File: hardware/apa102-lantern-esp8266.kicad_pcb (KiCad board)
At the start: 2 copper layers, 63.5 x 63.5 mm, 26 parts, among them P1 CONN_01X02, P10 CONN_01X06, P2 CONN_01X06, P3 CONN_01X06, P4 CONN_01X06, P5 CONN_01X06, P6 CONN_01X06, P7 CONN_01X06, P8 CONN_01X06, P9 CONN_01X06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

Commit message: Adds github url to pcbs
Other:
- board text added: "github.com/ Nervengift/ apa102lantern"
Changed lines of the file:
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@@
 (kicad_pcb (version 4) (host pcbnew "(2015-09-28 BZR 6225)-product")
   (general
-    (links 0)
-    (no_connects 0)
+    (links 55)
+    (no_connects 1)
     (area 133.299999 63.449999 196.900001 127.050001)
     (thickness 1.6)
-    (drawings 16)
+    (drawings 17)
     (tracks 141)
     (zones 0)
@@
       (net 2 GND))
   )
+  (gr_text "github.com/\nNervengift/\napa102lantern" (at 165.1 123.19) (layer B.SilkS)
+    (effects (font (size 1 1) (thickness 0.1)) (justify mirror))
+  )
   (gr_text 5V (at 180.721 91.44) (layer B.SilkS)

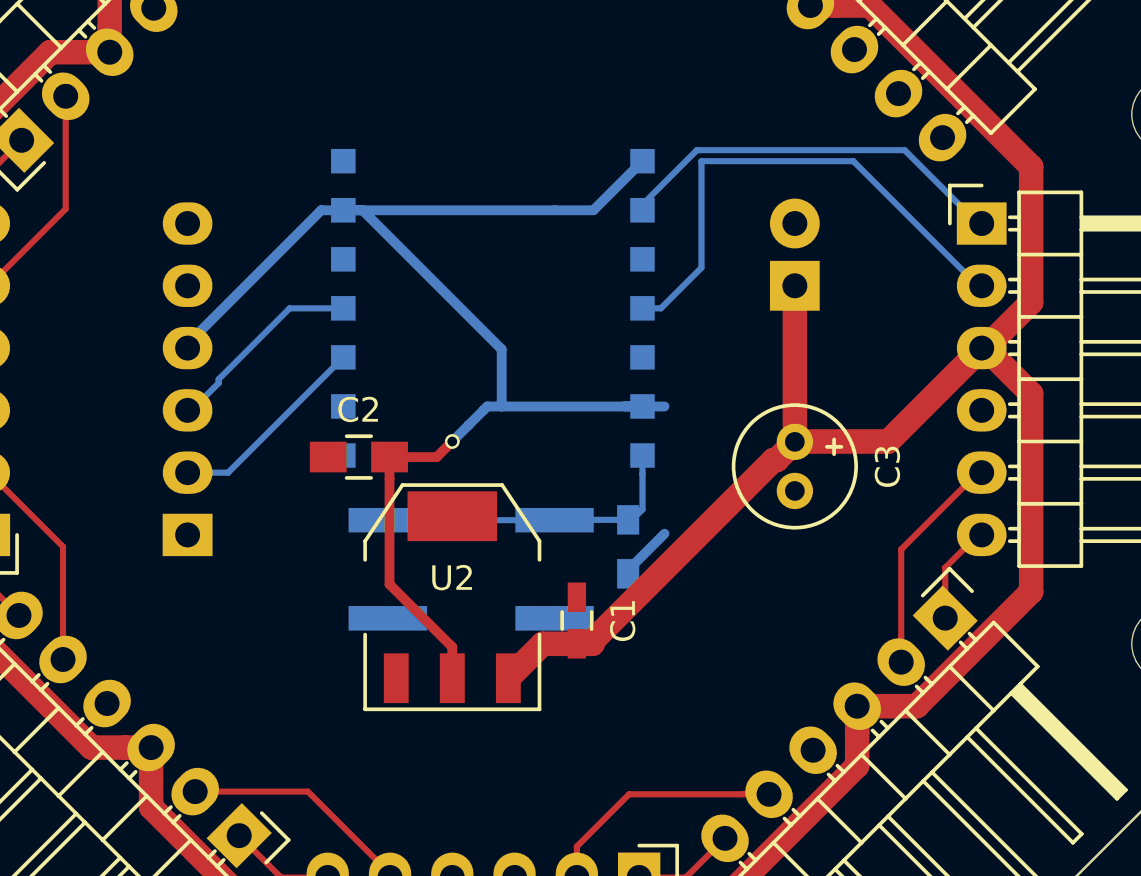
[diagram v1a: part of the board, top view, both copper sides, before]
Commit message: Adds pins to access the leds directly via SPI
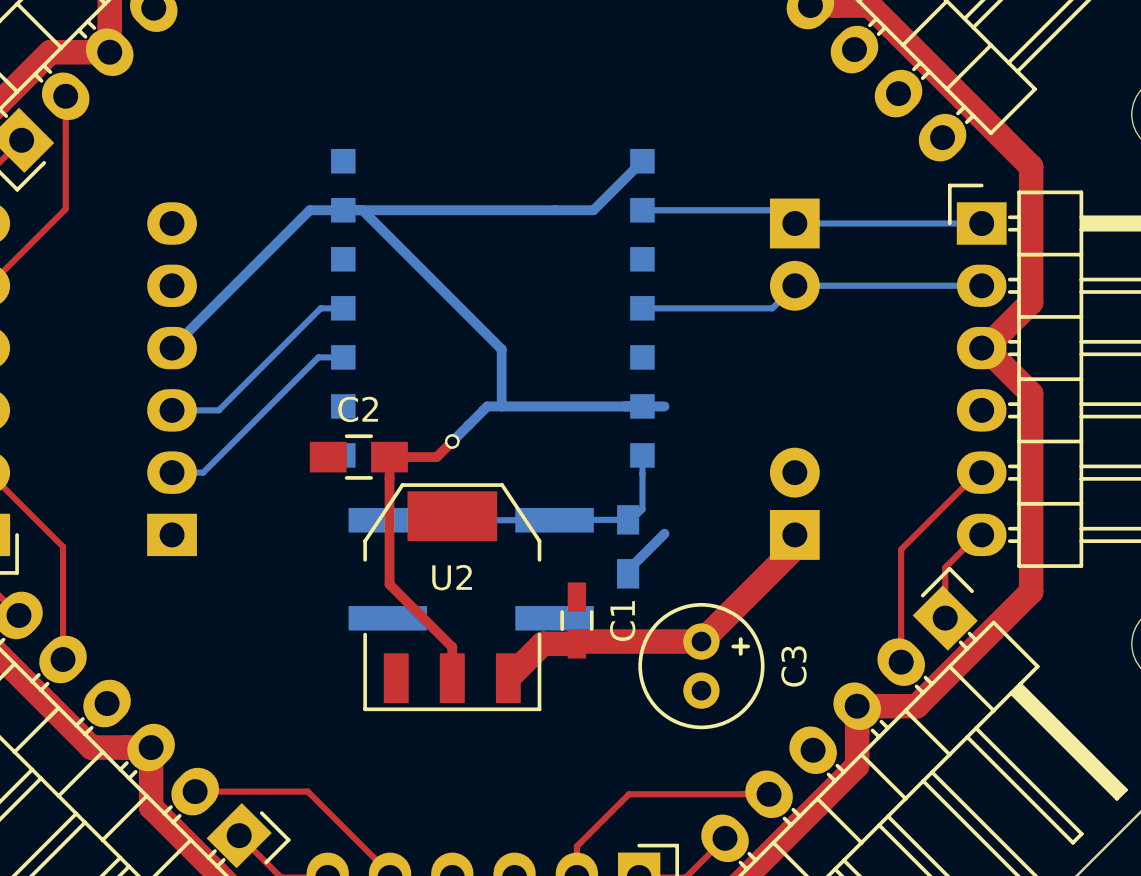
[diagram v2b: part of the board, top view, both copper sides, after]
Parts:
- added P11: CONN_01X02, Pin_Headers:Pin_Header_Straight_1x02, B.Cu at (177.8, 88.9)
- moved P1 10.2 mm to (177.8, 101.6)
- moved C3 8.99 mm to (174.0, 105.9)
- moved P2 0.63 mm to (152.4, 101.6)
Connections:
- net Net-(P3-Pad1) renamed /CLK
- net Net-(P3-Pad2) renamed /MOSI
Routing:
- net VCC: track 189.9 -> 173.1 mm
- net /MOSI: track 21.0 -> 14.4 mm
- net /CLK: track 16.2 -> 14.2 mm
- net /TX: track 8.30 -> 8.93 mm
- net /RX: track 8.16 -> 8.71 mm
- net +3V3: track 58.1 -> 58.6 mm
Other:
- net class 3v3 added: clearance 0.2, trace_width 0.4, via_dia 0.6, via_drill 0.4
- net class Default: trace_width 0.4 -> 0.25
- board text added: "CLK"
- board text added: "DATA"

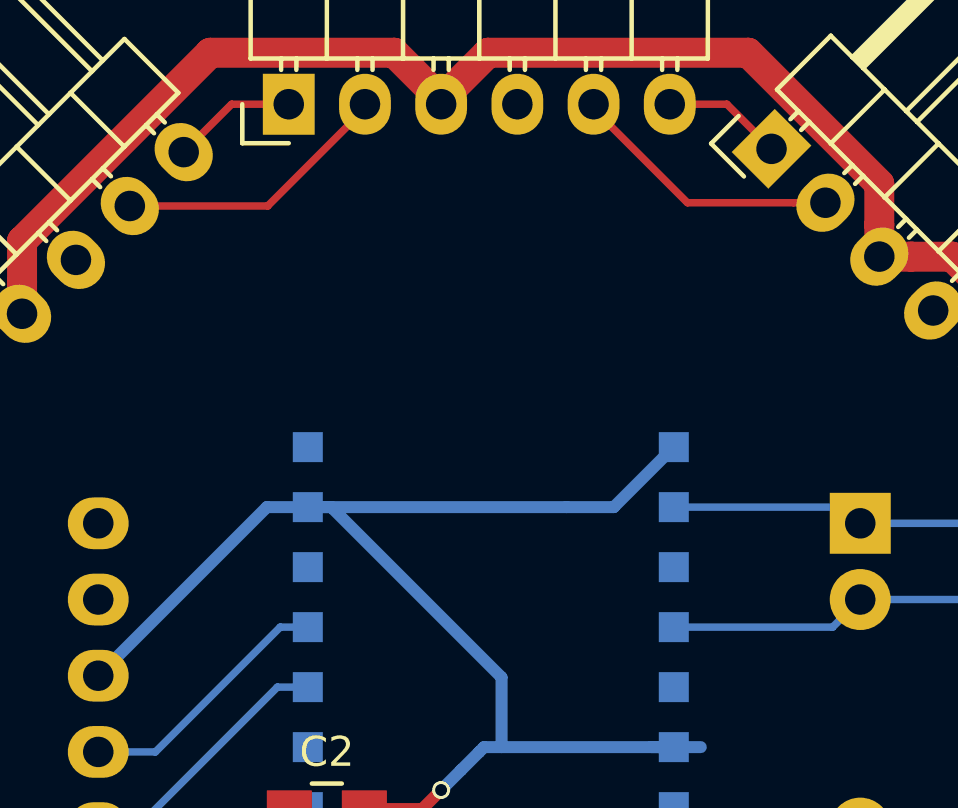
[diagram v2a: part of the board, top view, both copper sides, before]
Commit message: Adds license to esp board silkscreen
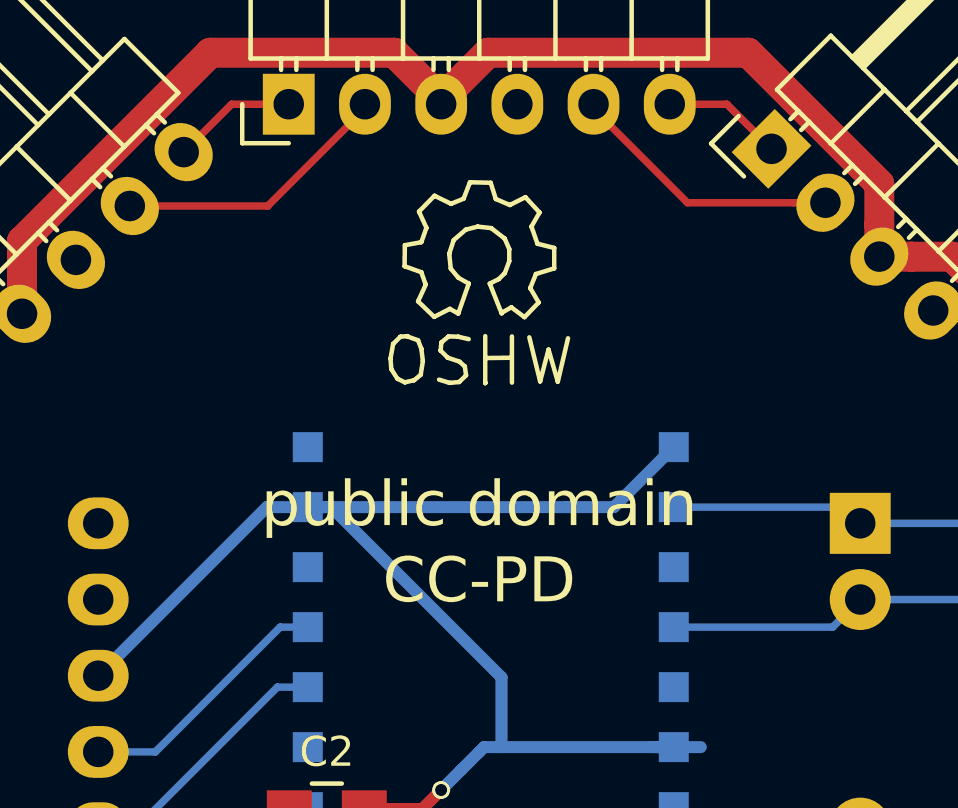
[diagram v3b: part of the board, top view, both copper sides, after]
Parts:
- REF**: moved to F.Cu
- moved REF** 29.2 mm to (165.1, 80.0), turned to 0 degrees
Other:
- board text added: "CC-PD"
- board text added: "public domain"

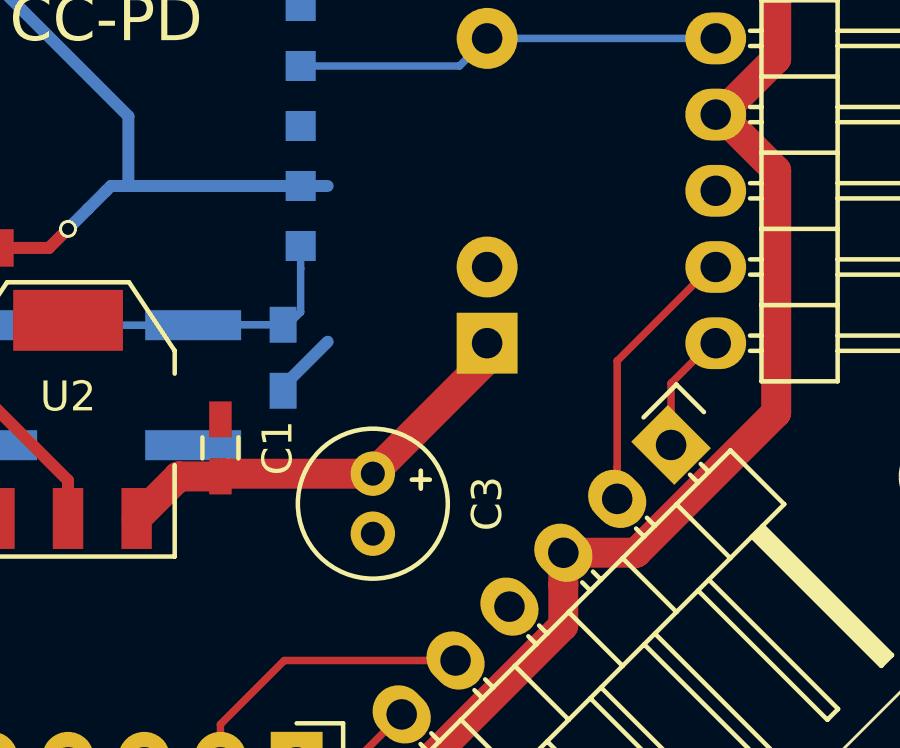
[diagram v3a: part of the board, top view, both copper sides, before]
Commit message: Fixes traces that where lost somehow
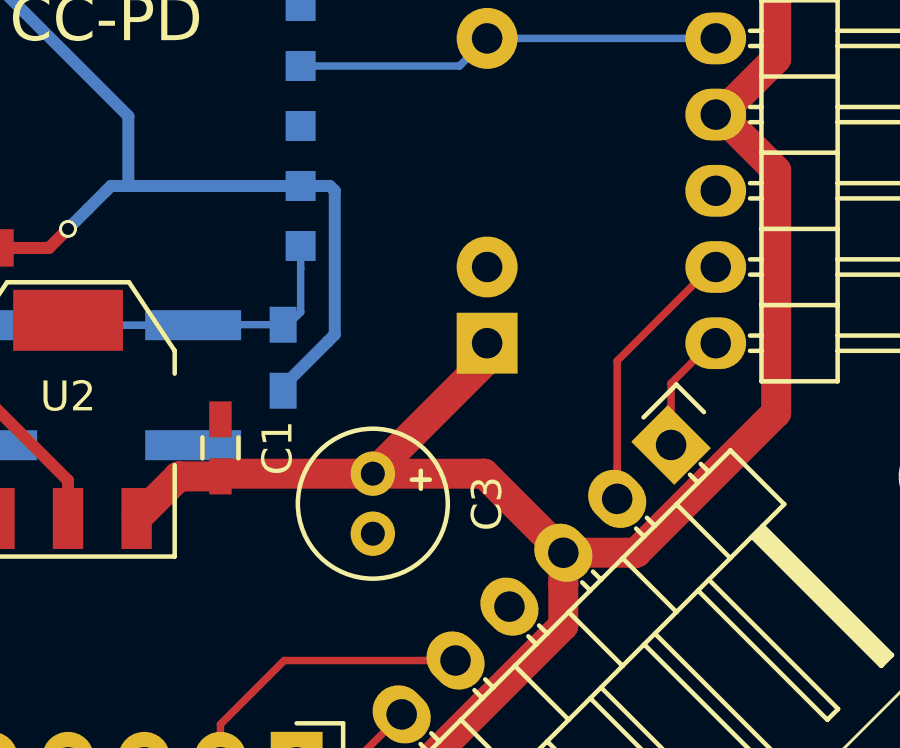
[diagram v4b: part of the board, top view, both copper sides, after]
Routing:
- net VCC: track 173.1 -> 180.5 mm
- net +3V3: track 58.6 -> 64.0 mm
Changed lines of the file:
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@@
 (kicad_pcb (version 4) (host pcbnew "(2015-09-28 BZR 6225)-product")
   (general
-    (links 0)
-    (no_connects 2)
+    (links 57)
+    (no_connects 0)
     (area 133.299999 63.449999 196.900001 127.050001)
     (thickness 1.6)
     (drawings 21)
-    (tracks 132)
+    (tracks 138)
     (zones 0)
     (modules 27)
@@
   (gr_line (start 177.8 127) (end 196.85 107.95) (layer Edge.Cuts) (width 0.1))
   (gr_line (start 152.4 127) (end 177.8 127) (layer Edge.Cuts) (width 0.1))
+  (segment (start 173.99 105.94848) (end 177.70348 105.94848) (width 1) (layer F.Cu) (net 1))
+  (segment (start 177.70348 105.94848) (end 180.34 108.585) (width 1) (layer F.Cu) (net 1))
   (segment (start 173.99 105.94848) (end 169.00152 105.94848) (width 1) (layer F.Cu) (net 1))
   (segment (start 169.00152 105.94848) (end 168.91 106.04) (width 1) (layer F.Cu) (net 1))
@@
   (segment (start 180.34 111.011806) (end 180.34 109.647346) (width 1) (layer F.Cu) (net 1))
   (segment (start 180.34 109.647346) (end 180.34 108.585) (width 1) (layer F.Cu) (net 1))
+  (segment (start 172.72 96.52) (end 172.72 101.315298) (width 0.4) (layer B.Cu) (net 3))
+  (segment (start 172.72 101.315298) (end 172.485001 101.550297) (width 0.4) (layer B.Cu) (net 3))
+  (segment (start 172.56 96.36) (end 172.72 96.52) (width 0.4) (layer B.Cu) (net 3))
+  (segment (start 172.485 96.36) (end 172.56 96.36) (width 0.4) (layer B.Cu) (net 3))
   (segment (start 158.02 88.36) (end 152.4 93.98) (width 0.4) (layer B.Cu) (net 3))
   (segment (start 159.385 88.36) (end 158.02 88.36) (width 0.4) (layer B.Cu) (net 3))

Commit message: Silkscreen fixes
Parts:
- renumbered R5 to R1
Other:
- board text added: "boot flash"
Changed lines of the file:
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@@
     (area 133.299999 63.449999 196.900001 127.050001)
     (thickness 1.6)
-    (drawings 21)
+    (drawings 22)
     (tracks 138)
     (zones 0)
@@
     (descr "Through hole pin header")
     (tags "pin header")
-    (fp_text reference P1 (at 0 3.048) (layer B.SilkS)
+    (fp_text reference P1 (at 0 3.048) (layer B.SilkS) hide
       (effects (font (size 1 1) (thickness 0.15)) (justify mirror))
     )
@@
     (tags "resistor 0603")
     (attr smd)
-    (fp_text reference R5 (at 0 -2.256188 270) (layer B.SilkS)
+    (fp_text reference R1 (at 0 -2.256188 270) (layer B.SilkS)
       (effects (font (size 1 1) (thickness 0.15)) (justify mirror))
     )
@@
     (descr "Through hole pin header")
     (tags "pin header")
-    (fp_text reference P2 (at 0 3.048) (layer B.SilkS)
+    (fp_text reference P2 (at 0 3.048) (layer B.SilkS) hide
       (effects (font (size 1 1) (thickness 0.15)) (justify mirror))
     )
@@
       (effects (font (size 1 1) (thickness 0.15)))
     )
-    (fp_text value 100u (at 1.016 5.08 270) (layer F.Fab)
+    (fp_text value 100u (at 1.06676 -0.01 360) (layer F.Fab)
       (effects (font (size 1 1) (thickness 0.15)))
     )
@@
     (descr "Light Touch Switch")
     (attr smd)
-    (fp_text reference SW1 (at -1 4 180) (layer B.SilkS)
+    (fp_text reference SW1 (at 6.6 0 180) (layer B.SilkS)
       (effects (font (size 1 1) (thickness 0.15)) (justify mirror))
     )
@@
     (descr "Through hole pin header")
     (tags "pin header")
-    (fp_text reference P11 (at 0 5.1 180) (layer B.SilkS)
+    (fp_text reference P11 (at 0 5.1 180) (layer B.SilkS) hide
       (effects (font (size 1 1) (thickness 0.15)) (justify mirror))
     )
@@
     )
   )
+  (gr_text "boot flash" (at 164.5 107.5) (layer B.SilkS)
+    (effects (font (size 1 1) (thickness 0.1)) (justify mirror))
+  )
   (gr_text CC-PD (at 165.1 90.805) (layer F.SilkS)

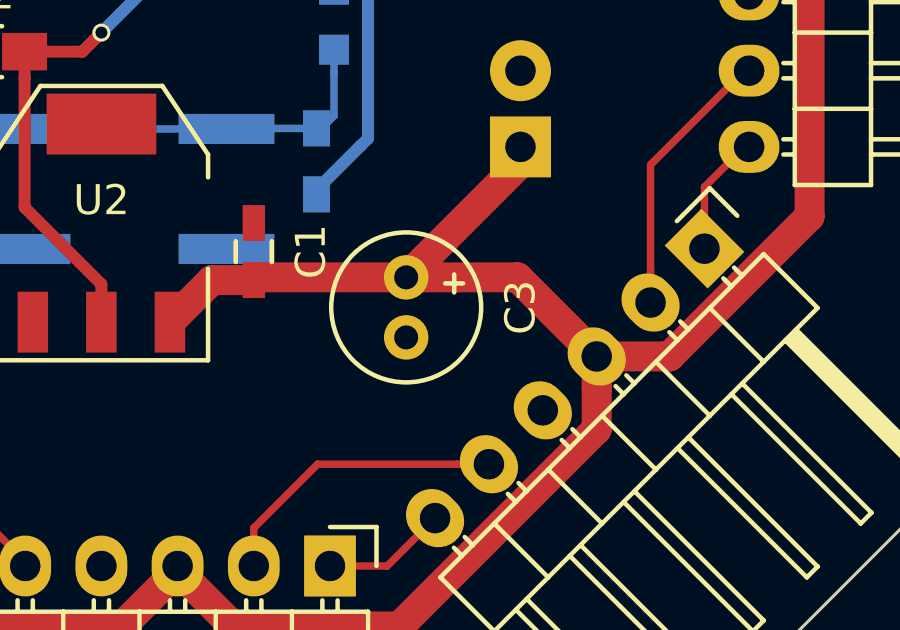
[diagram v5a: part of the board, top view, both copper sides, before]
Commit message: Bigger footprint for C3
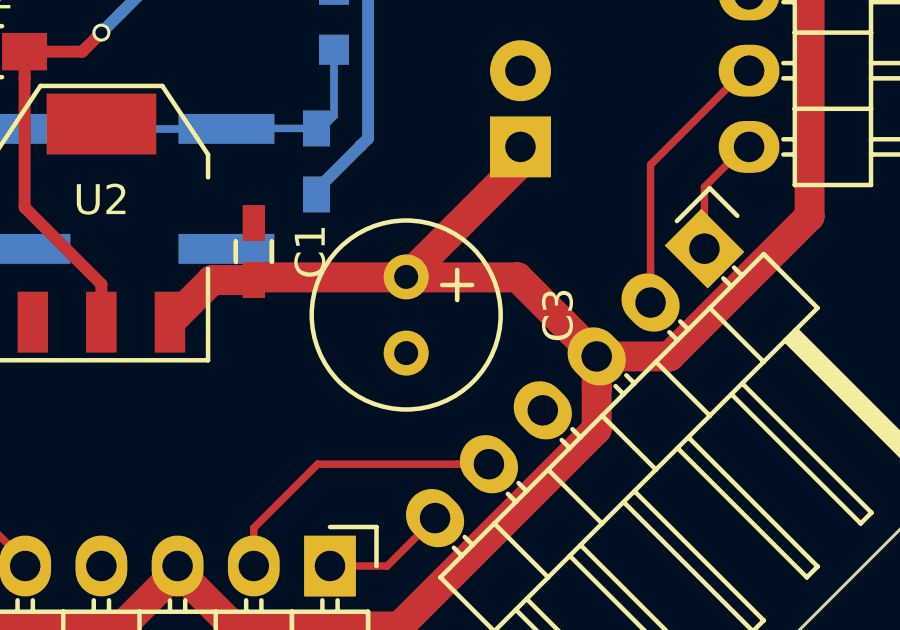
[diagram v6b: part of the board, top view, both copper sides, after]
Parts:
- C3: footprint Capacitors_Elko_ThroughHole:Elko_vert_11x5mm_RM2 -> Capacitors_Elko_ThroughHole:Elko_vert_11.2x6.3mm_RM2.5
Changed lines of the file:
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@@
   (general
     (links 57)
-    (no_connects 0)
+    (no_connects 1)
     (area 133.299999 63.449999 196.900001 127.050001)
     (thickness 1.6)
@@
     (pad 1 thru_hole circle (at 0 0) (size 3 3) (drill 3) (layers))
   )
-  (module Capacitors_Elko_ThroughHole:Elko_vert_11x5mm_RM2 (layer F.Cu)
-    (at 173.99 105.93324 270)
-    (descr "Electrolytic Capacitor, vertical, diameter 5mm, RM 2mm, radial,")
-    (tags "Electrolytic Capacitor, vertical, diameter 5mm,  radial, RM 2mm, Elko, Electrolytkondensator, Kondensator gepolt, Durchmesser 5mm")
-    (fp_text reference C3 (at 1.016 -3.81 270) (layer F.SilkS)
-      (effects (font (size 1 1) (thickness 0.15)))
-    )
-    (fp_text value 100u (at 1.06676 -0.01 360) (layer F.Fab)
-      (effects (font (size 1 1) (thickness 0.15)))
-    )
-    (fp_line (start 0.2159 -1.89992) (end 0.2159 -1.30048) (layer F.SilkS) (width 0.15))
-    (fp_line (start -0.08382 -1.6002) (end 0.51562 -1.6002) (layer F.SilkS) (width 0.15))
-    (fp_line (start 0.2159 -1.6002) (end 0.2159 -1.30048) (layer F.Cu) (width 0.15))
-    (fp_line (start 0.2159 -1.6002) (end 0.51562 -1.6002) (layer F.Cu) (width 0.15))
-    (fp_line (start -0.08382 -1.6002) (end 0.2159 -1.6002) (layer F.Cu) (width 0.15))
-    (fp_line (start 0.2159 -1.6002) (end 0.2159 -1.89992) (layer F.Cu) (width 0.15))
-    (fp_circle (center 1.016 0) (end 3.51536 0) (layer F.SilkS) (width 0.15))
-    (pad 1 thru_hole circle (at 0.01524 0 270) (size 1.48082 1.48082) (drill 0.8001) (layers *.Cu *.Mask F.SilkS)
-      (net 1 VCC))
-    (pad 2 thru_hole circle (at 2.01676 0 270) (size 1.48082 1.48082) (drill 0.8001) (layers *.Cu *.Mask F.SilkS)
-      (net 2 GND))
-    (model Capacitors_Elko_ThroughHole.3dshapes/Elko_vert_11x5mm_RM2.wrl
-      (at (xyz 0 0 0))
-      (scale (xyz 1 1 1))
-      (rotate (xyz 0 0 0))
-    )
-  )
   (module Buttons_Switches_SMD:SW_SPST_EVQP0 (layer B.Cu)
     (at 164.6 103 180)
@@
     )
   )
+  (module Capacitors_Elko_ThroughHole:Elko_vert_11.2x6.3mm_RM2.5 (layer F.Cu)
+    (at 173.99 105.93324 270)
+    (descr "Electrolytic Capacitor, vertical, diameter 6,3mm, RM 2,5mm, radial,")
+    (tags "Electrolytic Capacitor, vertical, diameter 6,3mm, RM 2,5mm, Elko, Electrolytkondensator, Kondensator gepolt, Durchmesser 6,3mm, radial,")
+    (fp_text reference C3 (at 1.27 -5.08 270) (layer F.SilkS)
+      (effects (font (size 1 1) (thickness 0.15)))
+    )
+    (fp_text value 100u (at 1.27 -0.01 360) (layer F.Fab)
+      (effects (font (size 1 1) (thickness 0.15)))
+    )
+    (fp_line (start 0.26924 -2.19964) (end 0.26924 -1.19888) (layer F.SilkS) (width 0.15))
+    (fp_line (start -0.23114 -1.69926) (end 0.76962 -1.69926) (layer F.SilkS) (width 0.15))
+    (fp_line (start 0.26924 -1.69926) (end 0.76962 -1.69926) (layer F.Cu) (width 0.15))
+    (fp_line (start 0.26924 -1.69926) (end 0.26924 -2.19964) (layer F.Cu) (width 0.15))
+    (fp_line (start -0.23114 -1.69926) (end 0.26924 -1.69926) (layer F.Cu) (width 0.15))
+    (fp_line (start 0.26924 -1.69926) (end 0.26924 -1.30048) (layer F.Cu) (width 0.15))
+    (fp_line (start 0.26924 -1.30048) (end 0.26924 -1.19888) (layer F.Cu) (width 0.15))
+    (fp_circle (center 1.27 0) (end 4.4196 0) (layer F.SilkS) (width 0.15))
+    (pad 2 thru_hole circle (at 2.54 0 270) (size 1.50114 1.50114) (drill 0.8001) (layers *.Cu *.Mask F.SilkS)
+      (net 2 GND))
+    (pad 1 thru_hole circle (at 0 0 270) (size 1.50114 1.50114) (drill 0.8001) (layers *.Cu *.Mask F.SilkS)
+      (net 1 VCC))
+    (model Capacitors_Elko_ThroughHole.3dshapes/Elko_vert_11.2x6.3mm_RM2.5.wrl
+      (at (xyz 0 0 0))
+      (scale (xyz 1 1 1))
+      (rotate (xyz 0 0 0))
+    )
+  )
